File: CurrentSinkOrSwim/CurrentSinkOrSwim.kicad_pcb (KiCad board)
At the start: 2 copper layers, 41.7 x 47.8 mm, 22 parts, among them K101 CONN_3, P101 CONN_2, P102 CONN_2, P301 CONN_1, Q301 BUK7575, U201 LMV358, U401 LM2931ACDG

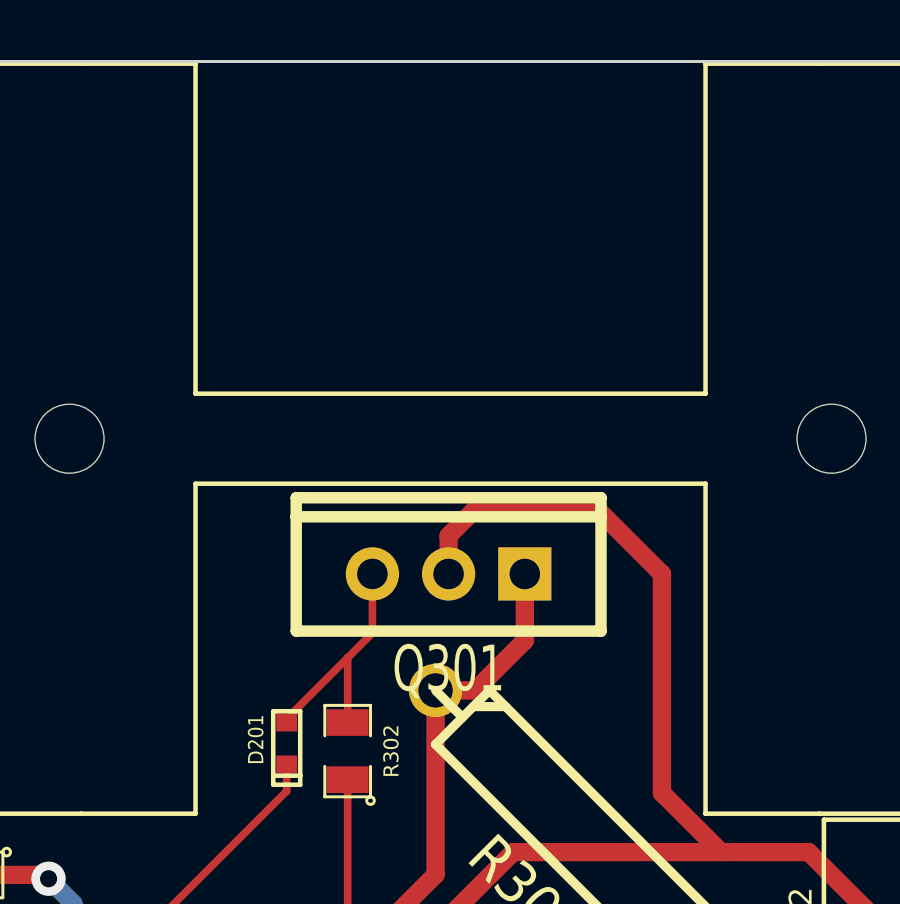
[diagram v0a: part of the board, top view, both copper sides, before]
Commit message: generando los ficheros Gerber y metiendo el logo
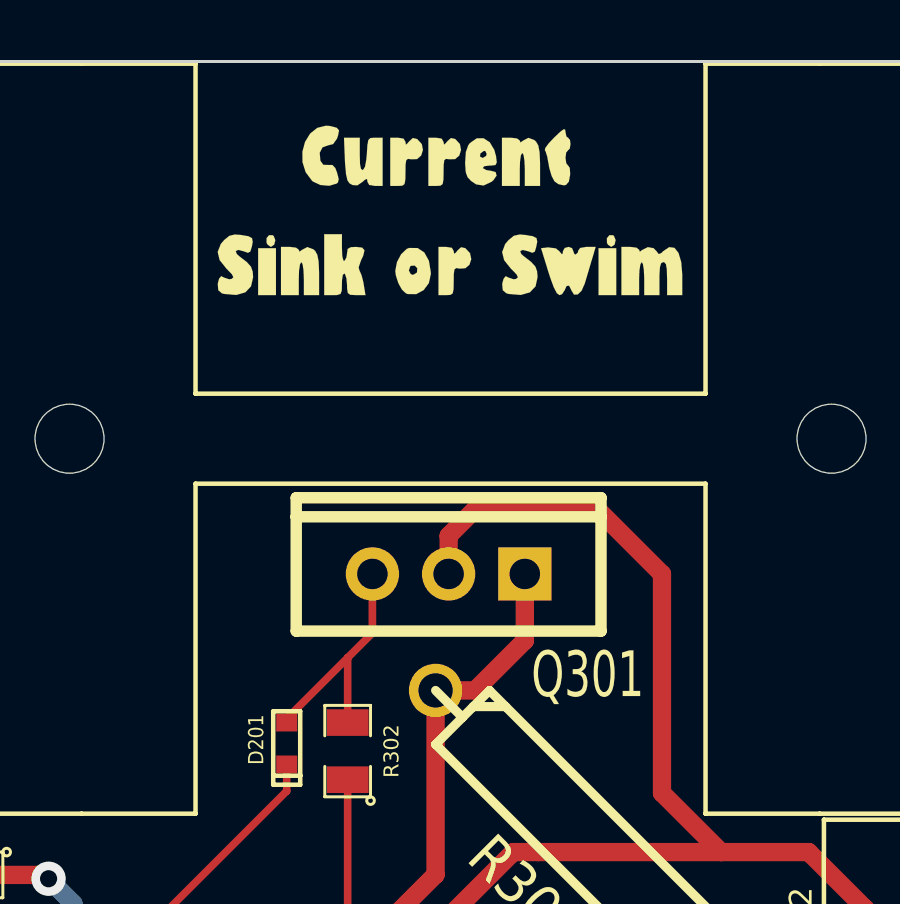
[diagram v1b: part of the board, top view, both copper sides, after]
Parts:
- added G***: Current_SOS_LOGO, LOGO_Final, F.Cu at (126.9, 40.9)
